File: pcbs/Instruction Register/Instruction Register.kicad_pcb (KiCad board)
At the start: 2 copper layers, 129.5 x 152.4 mm, 42 parts, among them J1001 Conn_02x20_Odd_Even, J1002 Conn_02x20_Odd_Even, U1001 74HC245, U1002 74HC245, U1003 74HC245, U1004 74HC245, U2001 74HC14, U2002 74HC08, U2003 74HC138, U3001 74HC245

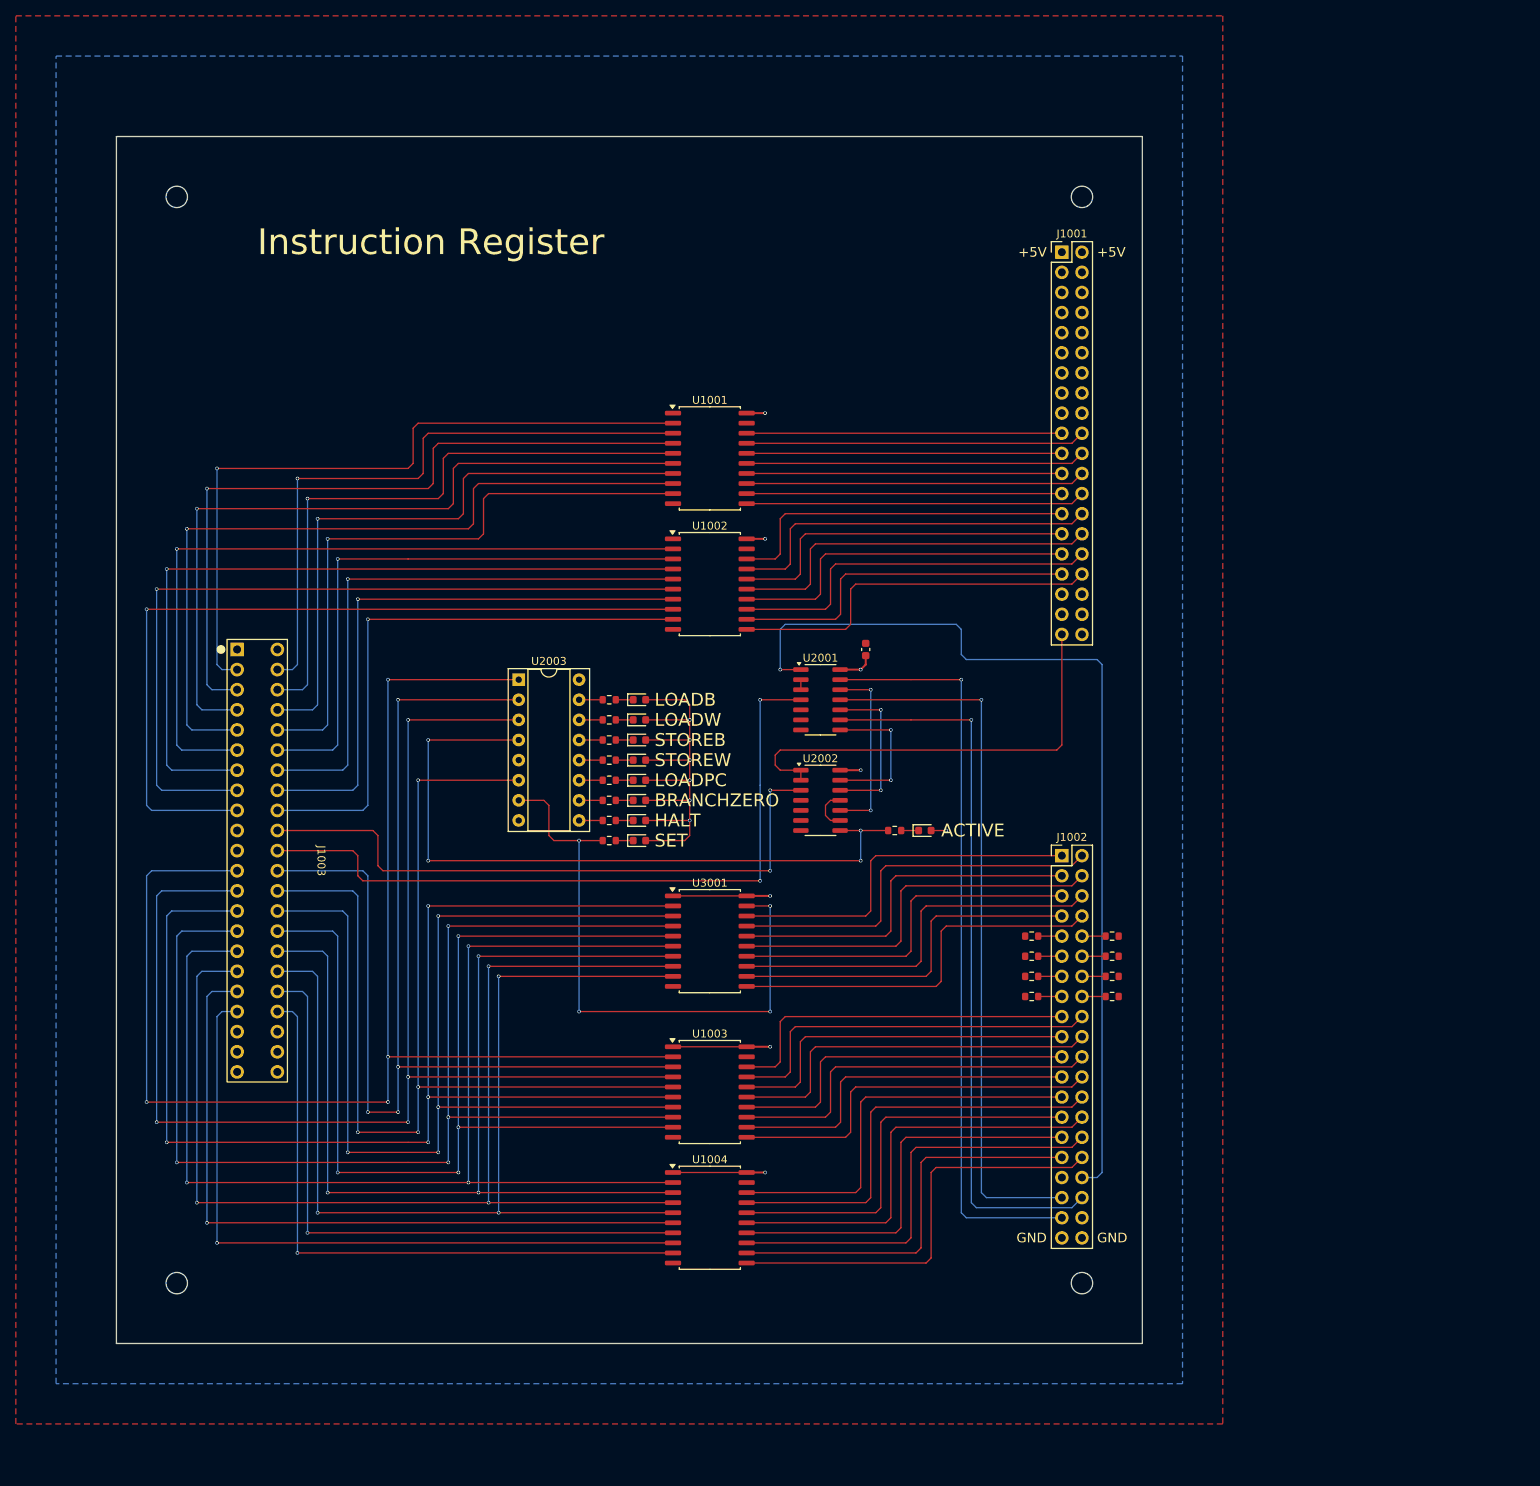
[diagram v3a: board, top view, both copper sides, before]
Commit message: Add name, shrink board slightly
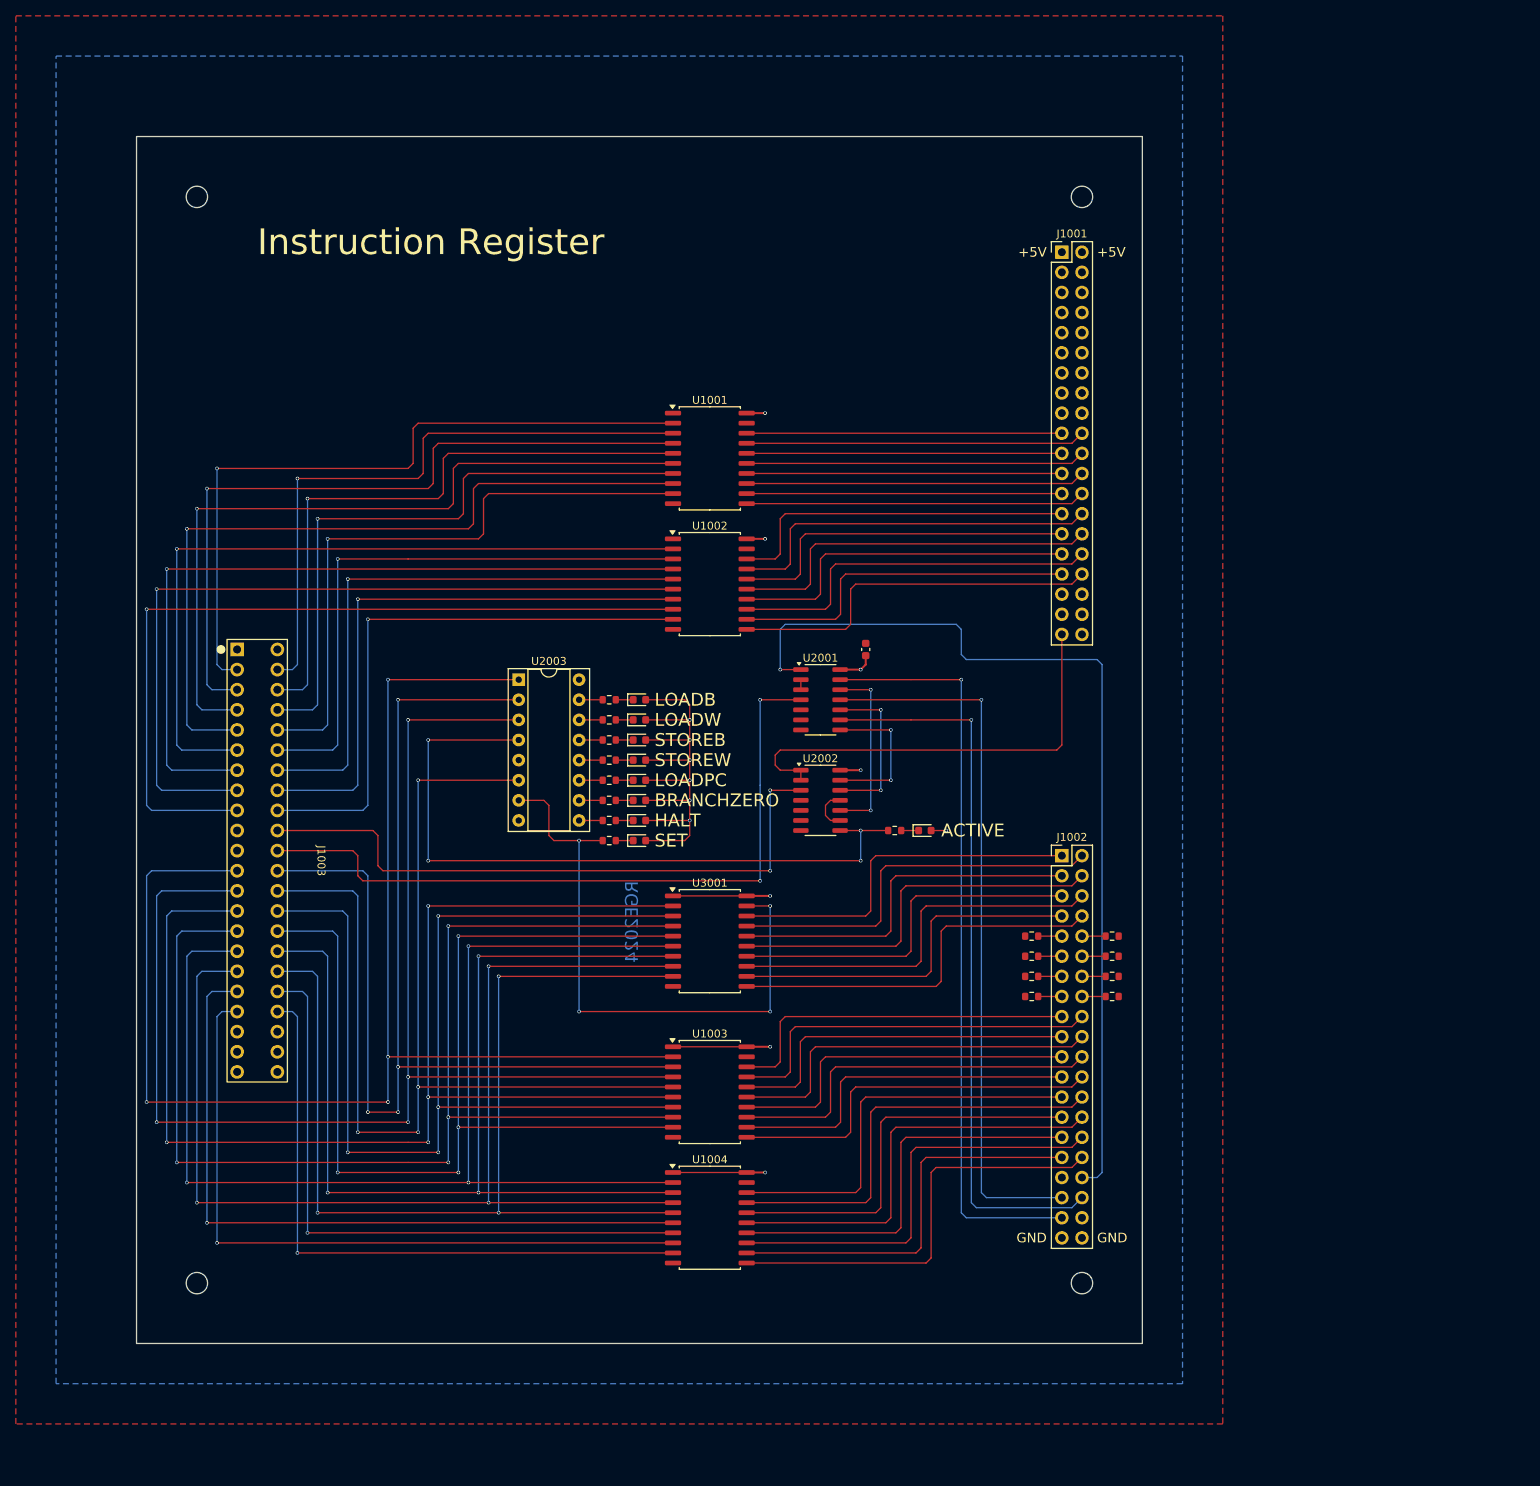
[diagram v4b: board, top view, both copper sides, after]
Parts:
- moved H1001 2.54 mm to (94.0, 43.2)
- moved H1004 2.54 mm to (94.0, 180.3)
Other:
- board size 129.5 x 152.4 mm -> 127 x 152.4 mm
- board text added: "RGE2024"
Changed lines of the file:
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@@
 	(footprint "MountingHole:MountingHole_2.7mm_M2.5_ISO7380"
 		(layer "F.Cu")
-		(at 91.44 43.18)
+		(at 93.98 43.18)
 		(descr "Mounting Hole 2.7mm, no annular, M2.5, ISO7380")
 		(tags "mounting hole 2.7mm no annular m2.5 iso7380")
@@
 	(footprint "MountingHole:MountingHole_2.7mm_M2.5_ISO7380"
 		(layer "F.Cu")
-		(at 91.44 180.34)
+		(at 93.98 180.34)
 		(descr "Mounting Hole 2.7mm, no annular, M2.5, ISO7380")
 		(tags "mounting hole 2.7mm no annular m2.5 iso7380")
@@
 	)
 	(gr_rect
-		(start 83.82 35.56)
+		(start 86.36 35.56)
 		(end 213.36 187.96)
 		(stroke
@@
 		(layer "Edge.Cuts")
 	)
+	(gr_text "RGE2024"
+		(at 149.86 129.54 90)
+		(layer "B.Cu")
+		(effects
+			(font
+				(size 1.6256 1.6256)
+				(thickness 0.2032)
+			)
+			(justify left bottom mirror)
+		)
+	)
 	(gr_text "JLCJLCJLCJLC"
 		(at 205.105 106.045 90)
@@
 		(min_thickness 0.127)
 		(filled_areas_thickness no)
-		(fill
+		(fill yes
 			(thermal_gap 0.5)
 			(thermal_bridge_width 0.5)
@@
 		(min_thickness 0.127)
 		(filled_areas_thickness no)
-		(fill
+		(fill yes
 			(thermal_gap 0.5)
 			(thermal_bridge_width 0.5)

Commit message: Final check and add more silkscreen
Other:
- board text added: "IR"
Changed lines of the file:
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@@
+		)
+	)
+	(gr_text "IR"
+		(at 101.6 160.02 0)
+		(layer "F.SilkS")
+		(effects
+			(font
+				(size 2.4384 2.4384)
+				(thickness 0.2032)
+			)
+			(justify bottom)
 		)
 	)
